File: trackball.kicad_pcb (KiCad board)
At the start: 2 copper layers, 27.5 x 35.2 mm, 37 parts, among them P1 CONN_10, P2 CONN_5, U1 MKL03Z32VFK4, U2 ADNS-3530, U4 ESD

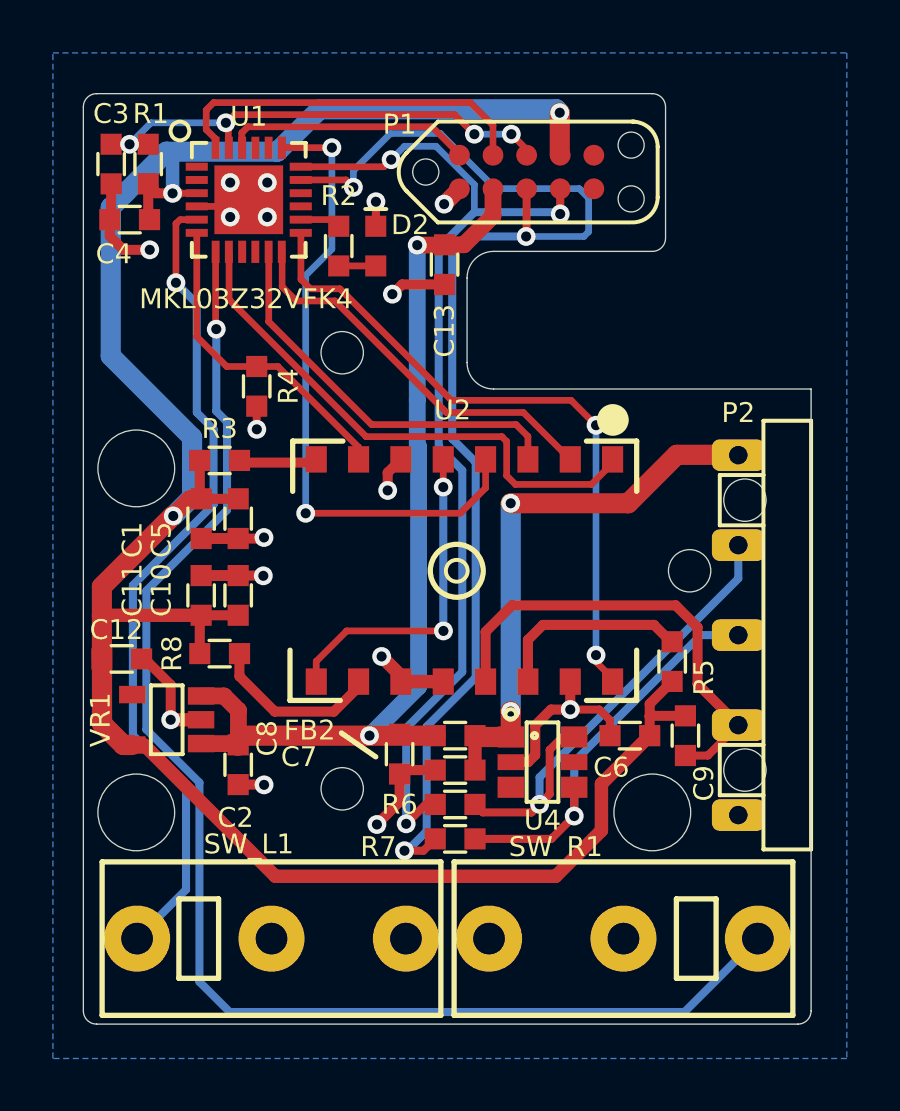
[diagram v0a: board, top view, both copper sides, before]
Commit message: Visible values on silkscreen.
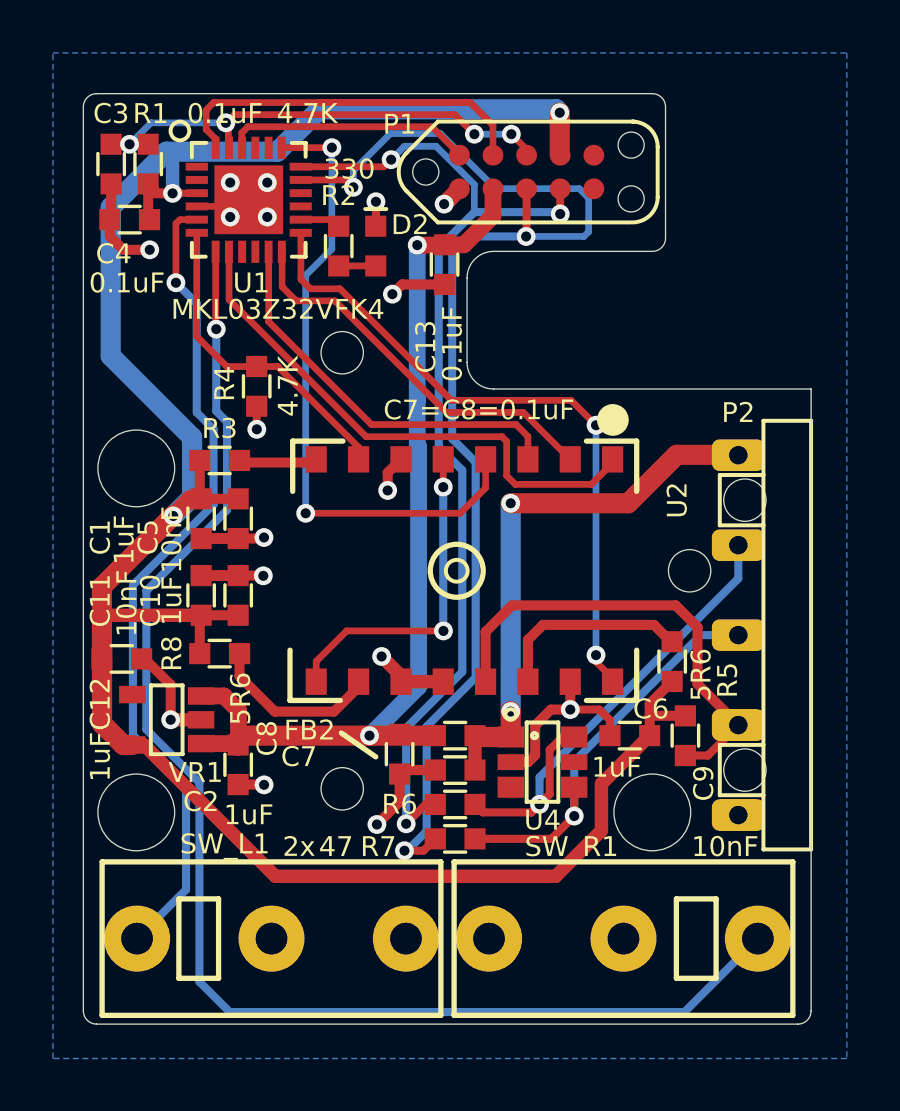
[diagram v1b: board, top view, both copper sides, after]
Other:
- board text added: "2x"
- board text added: "C7=C8=0.1uF"
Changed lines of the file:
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@@
   (general
     (thickness 1.6)
-    (drawings 41)
+    (drawings 43)
     (tracks 360)
     (zones 0)
@@
   (module ugl:ADNS-3530 locked (layer F.Cu)
     (at 196.260001 130.569003)
-    (fp_text reference U2 (at -0.160001 -6.069003) (layer F.SilkS)
+    (fp_text reference U2 (at 8.339999 -2.669003 90) (layer F.SilkS)
       (effects (font (size 0.746 0.746) (thickness 0.15)))
     )
@@
     (at 195.8 119 90)
     (attr smd)
-    (fp_text reference C13 (at -2.5 0 90) (layer F.SilkS)
-      (effects (font (size 0.75 0.75) (thickness 0.15)))
-    )
-    (fp_text value 0.1uF (at 0 1.5 90) (layer F.SilkS) hide
+    (fp_text reference C13 (at -3.1 -0.7 90) (layer F.SilkS)
+      (effects (font (size 0.75 0.75) (thickness 0.15)))
+    )
+    (fp_text value 0.1uF (at -3 0.3 90) (layer F.SilkS)
       (effects (font (size 0.75 0.75) (thickness 0.15)))
     )
@@
     (clearance 0.1)
     (attr smd)
-    (fp_text reference U1 (at 0 -3.15) (layer F.SilkS)
-      (effects (font (size 0.75 0.75) (thickness 0.15)))
-    )
-    (fp_text value MKL03Z32VFK4 (at -0.1 3.75) (layer F.SilkS)
+    (fp_text reference U1 (at 0.1 3.15) (layer F.SilkS)
+      (effects (font (size 0.75 0.75) (thickness 0.15)))
+    )
+    (fp_text value MKL03Z32VFK4 (at 1.1 4.15) (layer F.SilkS)
       (effects (font (size 0.75 0.75) (thickness 0.15)))
     )
@@
       (effects (font (size 0.75 0.75) (thickness 0.15)))
     )
-    (fp_text value 10nF (at 0 1.5 90) (layer F.SilkS) hide
+    (fp_text value 10nF (at -4.2 1.5 180) (layer F.SilkS)
       (effects (font (size 0.75 0.75) (thickness 0.15)))
     )
@@
     (at 186.6 131.5 270)
     (attr smd)
-    (fp_text reference C11 (at -0.2 2.6 270) (layer F.SilkS)
-      (effects (font (size 0.75 0.75) (thickness 0.15)))
-    )
-    (fp_text value 10nF (at 0 1.5 270) (layer F.SilkS) hide
+    (fp_text reference C11 (at 0.2 3.8 270) (layer F.SilkS)
+      (effects (font (size 0.75 0.75) (thickness 0.15)))
+    )
+    (fp_text value 10nF (at 0.3 2.8 270) (layer F.SilkS)
       (effects (font (size 0.75 0.75) (thickness 0.15)))
     )
@@
       (effects (font (size 0.75 0.75) (thickness 0.15)))
     )
-    (fp_text value 4.7K (at 0 1.5 90) (layer F.SilkS) hide
+    (fp_text value 4.7K (at 1.9 6 180) (layer F.SilkS)
       (effects (font (size 0.75 0.75) (thickness 0.15)))
     )
@@
       (effects (font (size 0.75 0.75) (thickness 0.15)))
     )
-    (fp_text value 330 (at 0 1.5 90) (layer F.SilkS) hide
+    (fp_text value 330 (at 2.9 0.4 180) (layer F.SilkS)
       (effects (font (size 0.75 0.75) (thickness 0.15)))
     )
@@
     (at 188 131.5 270)
     (attr smd)
-    (fp_text reference C10 (at -0.2 2.9 270) (layer F.SilkS)
-      (effects (font (size 0.75 0.75) (thickness 0.15)))
-    )
-    (fp_text value 1uF (at 0 1.5 270) (layer F.SilkS) hide
+    (fp_text reference C10 (at 0.2 3.3 270) (layer F.SilkS)
+      (effects (font (size 0.75 0.75) (thickness 0.15)))
+    )
+    (fp_text value 1uF (at 0.2 2.5 270) (layer F.SilkS)
       (effects (font (size 0.75 0.75) (thickness 0.15)))
     )
@@
     (at 188.7 123.6 270)
     (attr smd)
-    (fp_text reference R4 (at 0 -1.2 270) (layer F.SilkS)
-      (effects (font (size 0.75 0.75) (thickness 0.15)))
-    )
-    (fp_text value 4.7K (at 0 1.5 270) (layer F.SilkS) hide
+    (fp_text reference R4 (at -0.1 1.2 270) (layer F.SilkS)
+      (effects (font (size 0.75 0.75) (thickness 0.15)))
+    )
+    (fp_text value 4.7K (at 0 -1.2 90) (layer F.SilkS)
       (effects (font (size 0.75 0.75) (thickness 0.15)))
     )
@@
     (at 204.4 134 270)
     (attr smd)
-    (fp_text reference R5 (at 0.6 -1.2 90) (layer F.SilkS)
-      (effects (font (size 0.75 0.75) (thickness 0.15)))
-    )
-    (fp_text value 5R6 (at 0 1.5 270) (layer F.SilkS) hide
+    (fp_text reference R5 (at 0.7 -2.1 90) (layer F.SilkS)
+      (effects (font (size 0.75 0.75) (thickness 0.15)))
+    )
+    (fp_text value 5R6 (at 0.5 -1.1 90) (layer F.SilkS)
       (effects (font (size 0.75 0.75) (thickness 0.15)))
     )
@@
       (effects (font (size 0.75 0.75) (thickness 0.15)))
     )
-    (fp_text value 47 (at 0 1.5) (layer F.SilkS) hide
+    (fp_text value 47 (at -4.5 0.3 180) (layer F.SilkS)
       (effects (font (size 0.75 0.75) (thickness 0.15)))
     )
@@
       (effects (font (size 0.75 0.75) (thickness 0.15)))
     )
-    (fp_text value 5R6 (at 0 1.5 180) (layer F.SilkS) hide
+    (fp_text value 5R6 (at -0.8 -1.7 270) (layer F.SilkS)
       (effects (font (size 0.75 0.75) (thickness 0.15)))
     )
@@
     (at 186.6 128.6 90)
     (attr smd)
-    (fp_text reference C1 (at -0.8 -2.6 90) (layer F.SilkS)
-      (effects (font (size 0.75 0.75) (thickness 0.15)))
-    )
-    (fp_text value 1uF (at 0 1.5 90) (layer F.SilkS) hide
+    (fp_text reference C1 (at -0.7 -3.8 90) (layer F.SilkS)
+      (effects (font (size 0.75 0.75) (thickness 0.15)))
+    )
+    (fp_text value 1uF (at -0.8 -2.9 90) (layer F.SilkS)
       (effects (font (size 0.75 0.75) (thickness 0.15)))
     )
@@
     (at 183.6 133.9 180)
     (attr smd)
-    (fp_text reference C12 (at 0.2 1.1 180) (layer F.SilkS)
-      (effects (font (size 0.75 0.75) (thickness 0.15)))
-    )
-    (fp_text value 1uF (at 0 1.5 180) (layer F.SilkS) hide
+    (fp_text reference C12 (at 0.8 -1.7 270) (layer F.SilkS)
+      (effects (font (size 0.75 0.75) (thickness 0.15)))
+    )
+    (fp_text value 1uF (at 0.8 -3.7 270) (layer F.SilkS)
       (effects (font (size 0.75 0.75) (thickness 0.15)))
     )
@@
     (at 188 137.9 90)
     (attr smd)
-    (fp_text reference C2 (at -2 -0.1 180) (layer F.SilkS)
-      (effects (font (size 0.75 0.75) (thickness 0.15)))
-    )
-    (fp_text value 1uF (at 0 1.5 90) (layer F.SilkS) hide
+    (fp_text reference C2 (at -1.4 -1.4 180) (layer F.SilkS)
+      (effects (font (size 0.75 0.75) (thickness 0.15)))
+    )
+    (fp_text value 1uF (at -1.9 0.4 180) (layer F.SilkS)
       (effects (font (size 0.75 0.75) (thickness 0.15)))
     )
@@
       (effects (font (size 0.75 0.75) (thickness 0.15)))
     )
-    (fp_text value 0.1uF (at 0 1.5 90) (layer F.SilkS) hide
+    (fp_text value 0.1uF (at 1.9 4.3 180) (layer F.SilkS)
       (effects (font (size 0.75 0.75) (thickness 0.15)))
     )
@@
       (effects (font (size 0.75 0.75) (thickness 0.15)))
     )
-    (fp_text value 0.1uF (at 0 1.5) (layer F.SilkS) hide
+    (fp_text value 0.1uF (at -0.1 2.4) (layer F.SilkS)
       (effects (font (size 0.75 0.75) (thickness 0.15)))
     )
@@
     (at 188 128.6 90)
     (attr smd)
-    (fp_text reference C5 (at -0.8 -2.9 90) (layer F.SilkS)
-      (effects (font (size 0.75 0.75) (thickness 0.15)))
-    )
-    (fp_text value 10nF (at 0 1.5 90) (layer F.SilkS) hide
+    (fp_text reference C5 (at -0.7 -3.4 90) (layer F.SilkS)
+      (effects (font (size 0.75 0.75) (thickness 0.15)))
+    )
+    (fp_text value 10nF (at -0.8 -2.5 90) (layer F.SilkS)
       (effects (font (size 0.75 0.75) (thickness 0.15)))
     )
@@
     (at 202.8 136.8)
     (attr smd)
-    (fp_text reference C6 (at -0.7 1.2) (layer F.SilkS)
-      (effects (font (size 0.75 0.75) (thickness 0.15)))
-    )
-    (fp_text value 1uF (at 0 1.5) (layer F.SilkS) hide
+    (fp_text reference C6 (at 0.8 -1) (layer F.SilkS)
+      (effects (font (size 0.75 0.75) (thickness 0.15)))
+    )
+    (fp_text value 1uF (at -0.5 1.2) (layer F.SilkS)
       (effects (font (size 0.75 0.75) (thickness 0.15)))
     )
@@
     (tags SOT23)
     (attr smd)
-    (fp_text reference VR1 (at 0 2.5 270) (layer F.SilkS)
+    (fp_text reference VR1 (at 2 -1.1) (layer F.SilkS)
       (effects (font (size 0.75 0.75) (thickness 0.15)))
     )
@@
   (module ugl:CMI126603D08 locked (layer F.Cu)
     (at 202.560004 144.468997 180)
-    (fp_text reference SW_R1 (at 2.560004 3.468997) (layer F.SilkS)
+    (fp_text reference SW_R1 (at 1.960004 3.468997) (layer F.SilkS)
       (effects (font (size 0.75 0.75) (thickness 0.15)))
     )
@@
   (module ugl:CMI126603D08 locked (layer F.Cu)
     (at 189.260001 144.468997)
-    (fp_text reference SW_L1 (at -0.860001 -3.568997) (layer F.SilkS)
+    (fp_text reference SW_L1 (at -1.760001 -3.568997) (layer F.SilkS)
       (effects (font (size 0.75 0.75) (thickness 0.15)))
     )
@@
       (clearance 0.00001))
   )
+  (gr_text C7=C8=0.1uF (at 197.1 124.5) (layer F.SilkS)
+    (effects (font (size 0.738 0.738) (thickness 0.15014)))
+  )
   (gr_line (start 191.9 136.7) (end 193.2 137.6) (layer F.SilkS) (width 0.2))
+  (gr_text 2x (at 190.3 141) (layer F.SilkS)
+    (effects (font (size 0.738 0.738) (thickness 0.15148)))
+  )
   (gr_text "PCB ID: trackball_main_0.1.0" (at 195.9 146.8) (layer B.SilkS)
     (effects (font (size 0.75 0.75) (thickness 0.15)) (justify mirror))

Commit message: Change UPA header pinout.
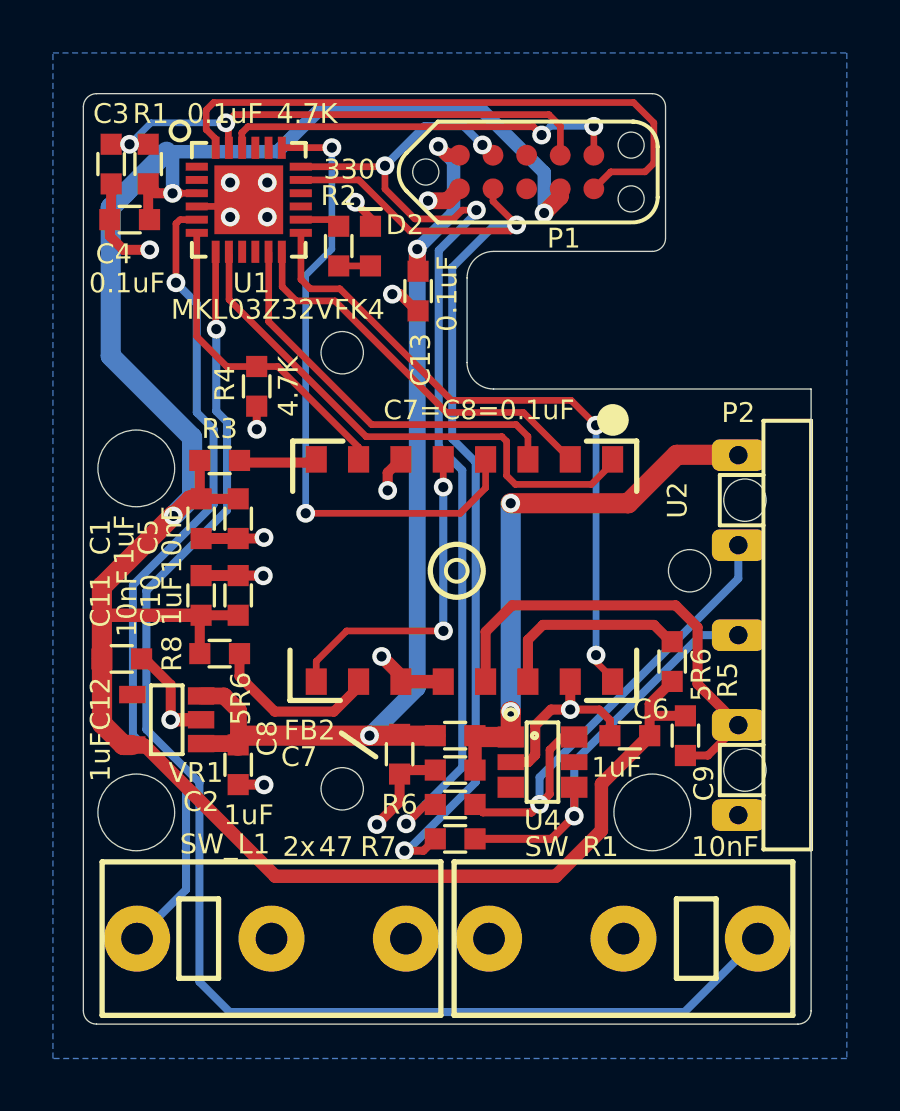
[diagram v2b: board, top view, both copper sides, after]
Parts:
- P1: footprint ugl:Tag_Connect_2x5_Header_With_No_Legs -> ugl:Tag_Connect_2x5_Header_With_No_Legs_Parallel_Numbering
- moved C13 1.41 mm to (194.8, 120.0)
- moved D2 0.20 mm to (193.0, 118.3)
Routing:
- net /SWDIO: track 14.0 -> 23.1 mm
- net /SCL: track 47.3 -> 39.0 mm, vias 3 -> 2
- net /SWDCLK: track 9.37 -> 15.4 mm, vias 0 -> 2
- net +5V: track 35.5 -> 37.5 mm, vias 2 -> 3
- net /RESET: track 18.6 -> 20.4 mm, vias 4 -> 2
- net +3V3: track 88.7 -> 90.2 mm
- net /SDA: track 39.1 -> 39.7 mm, vias 3 -> 4

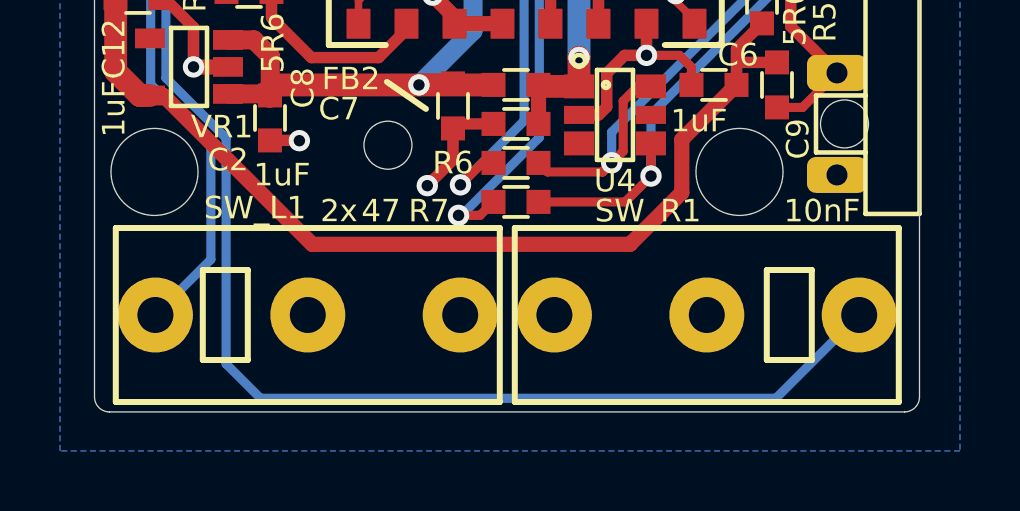
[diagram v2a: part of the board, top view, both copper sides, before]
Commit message: Update microswitch footprints.
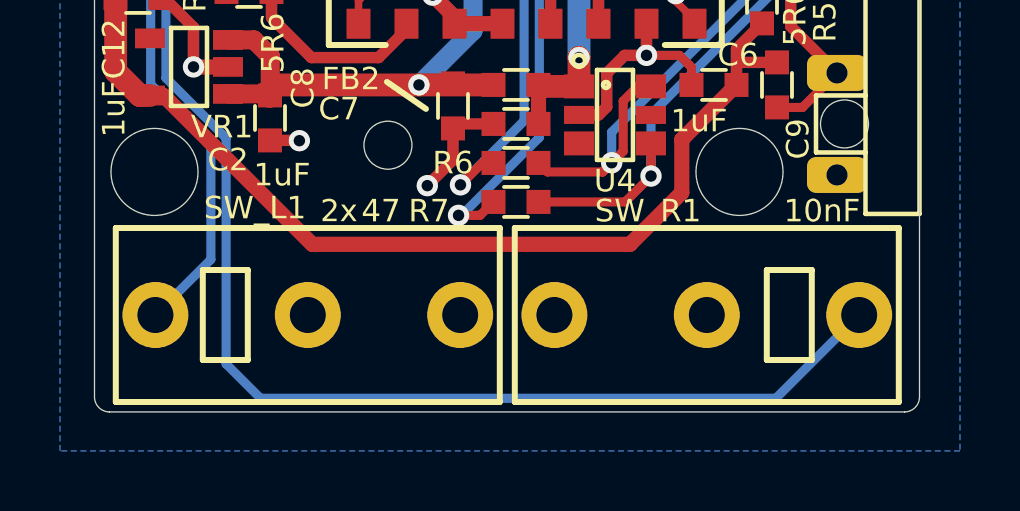
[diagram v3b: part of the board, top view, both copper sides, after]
